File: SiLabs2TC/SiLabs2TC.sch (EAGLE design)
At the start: 13 parts, among them U1 NCP1117LPST33T3G

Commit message: Major revamp of repo.
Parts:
- TC2030: LABEL01 GND -> (none); LABEL02 VCC -> (none); LABEL03 !RST!/C2CK -> (none); LABEL04 C2D -> (none)
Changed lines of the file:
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@@
 <?xml version="1.0" encoding="utf-8"?>
 <!DOCTYPE eagle SYSTEM "eagle.dtd">
-<eagle version="7.6.0">
+<eagle version="7.4.0">
 <drawing>
 <settings>
@@
 <part name="U$4" library="MF_Aesthetics" deviceset="GND_RAIL" device=""/>
 <part name="TC2030" library="PP_Connectors" deviceset="CON_02X03" device="_30306-6002HB" value="30306-6002HB">
-<attribute name="LABEL01" value="GND"/>
-<attribute name="LABEL02" value="VCC"/>
-<attribute name="LABEL03" value="!RST!/C2CK"/>
-<attribute name="LABEL04" value="C2D"/>
 <attribute name="LABEL05" value=""/>
 <attribute name="LABEL06" value=""/>

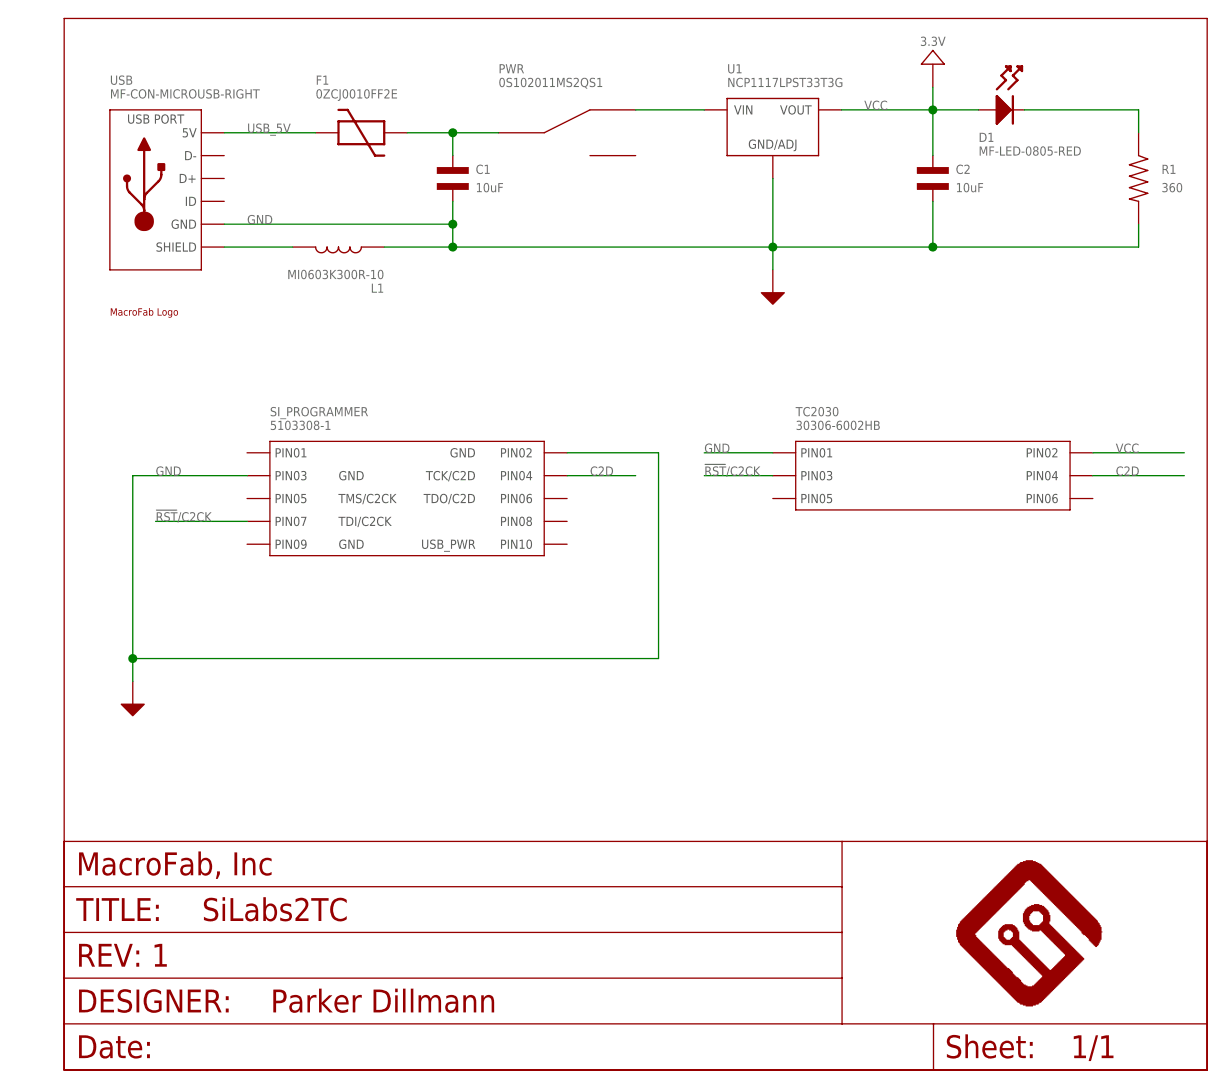
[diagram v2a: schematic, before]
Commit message: Added Pin sharing support for TagConnect.
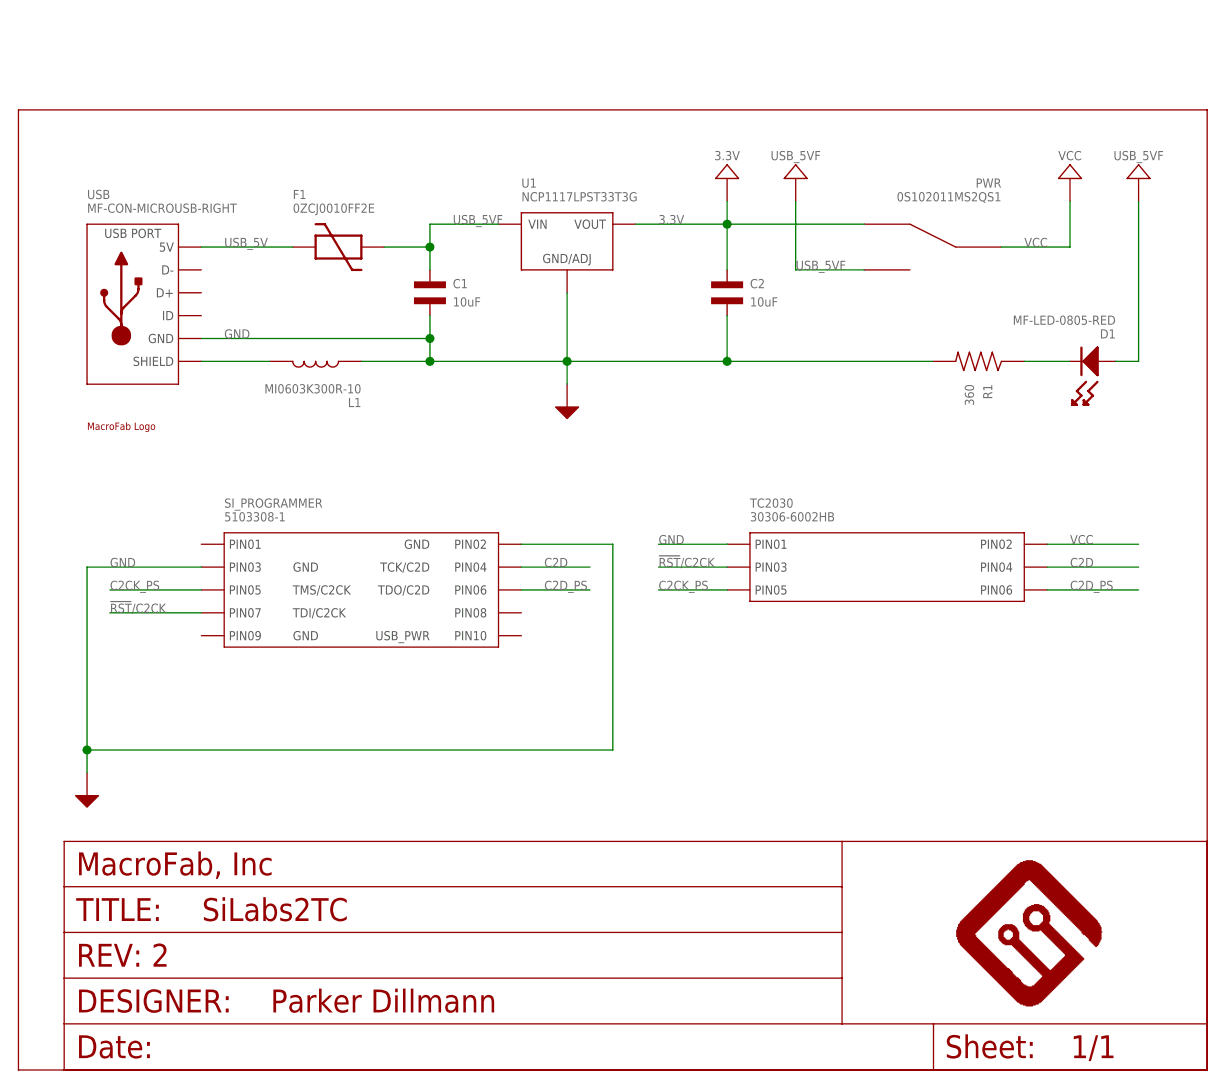
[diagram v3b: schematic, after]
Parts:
- FRAME1: REVNUM REV: 1 -> REV: 2
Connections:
- removed net N$2: C1.P$1, F1.P$2, PWR.C
- removed net N$5: PWR.1, U1.VIN
- new net 3.3V: C2.P$1, PWR.1, U1.VOUT
- new net C2CK_PS: SI_PROGRAMMER.PIN5, TC2030.PIN5
- new net C2D_PS: SI_PROGRAMMER.PIN6, TC2030.PIN6
- new net USB_5VF: C1.P$1, D1.ANODE, F1.P$2, PWR.2, U1.VIN
- net VCC: now also PWR.C; no longer C2.P$1, D1.ANODE, U1.VOUT
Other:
- moved on the sheet: C1, C2, D1, F1, L1, PWR, R1, SI_PROGRAMMER, TC2030, U1, USB
